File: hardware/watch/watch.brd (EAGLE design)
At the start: 36 x 35.5 mm, 92 parts, among them IC1 Digikey: WM9203CT-ND, IC2 MPR121, Q1 NTS4173, Q3 NTS4173, Q4 NTS4173, U1 Value, U10 2450BM14E0003, U11 MCP73831, U12 ML8511-UV-SENSORSMD, U13 LIGHTSENSORALS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

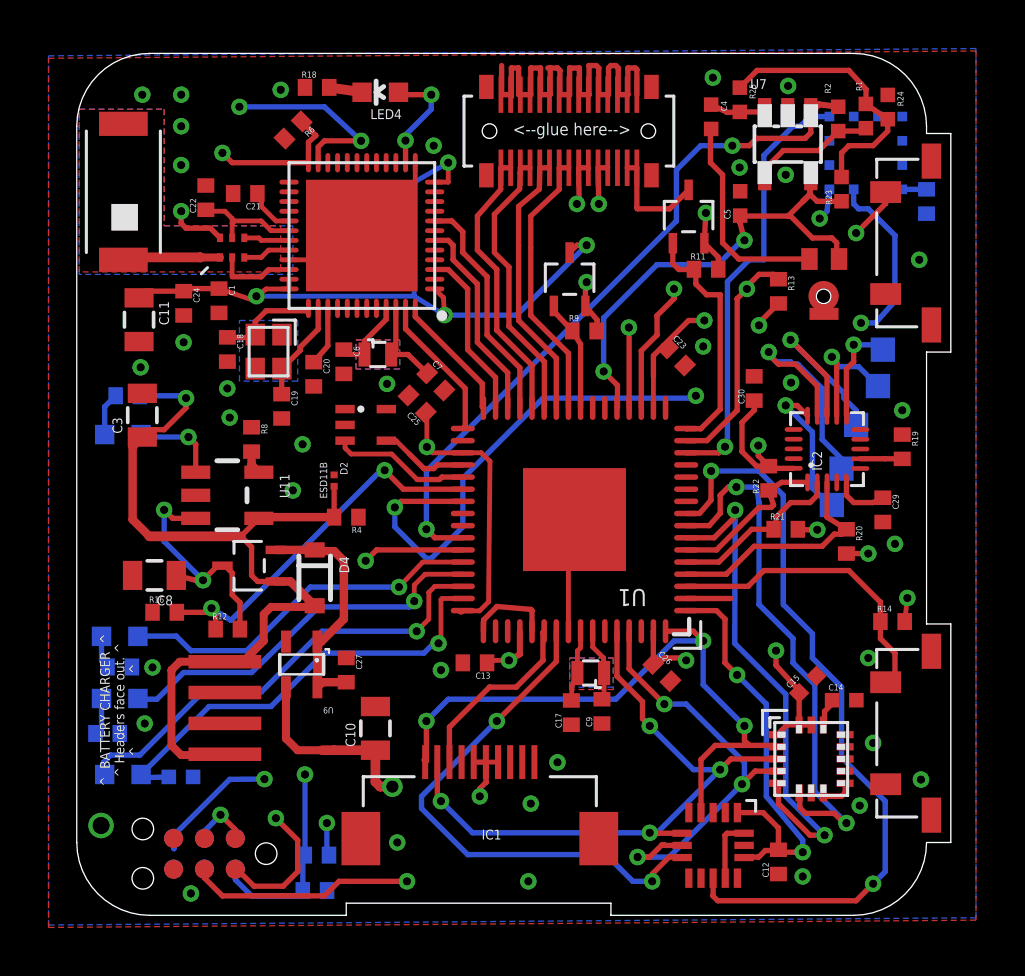
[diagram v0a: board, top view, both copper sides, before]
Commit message: New hardware revision, better connector.
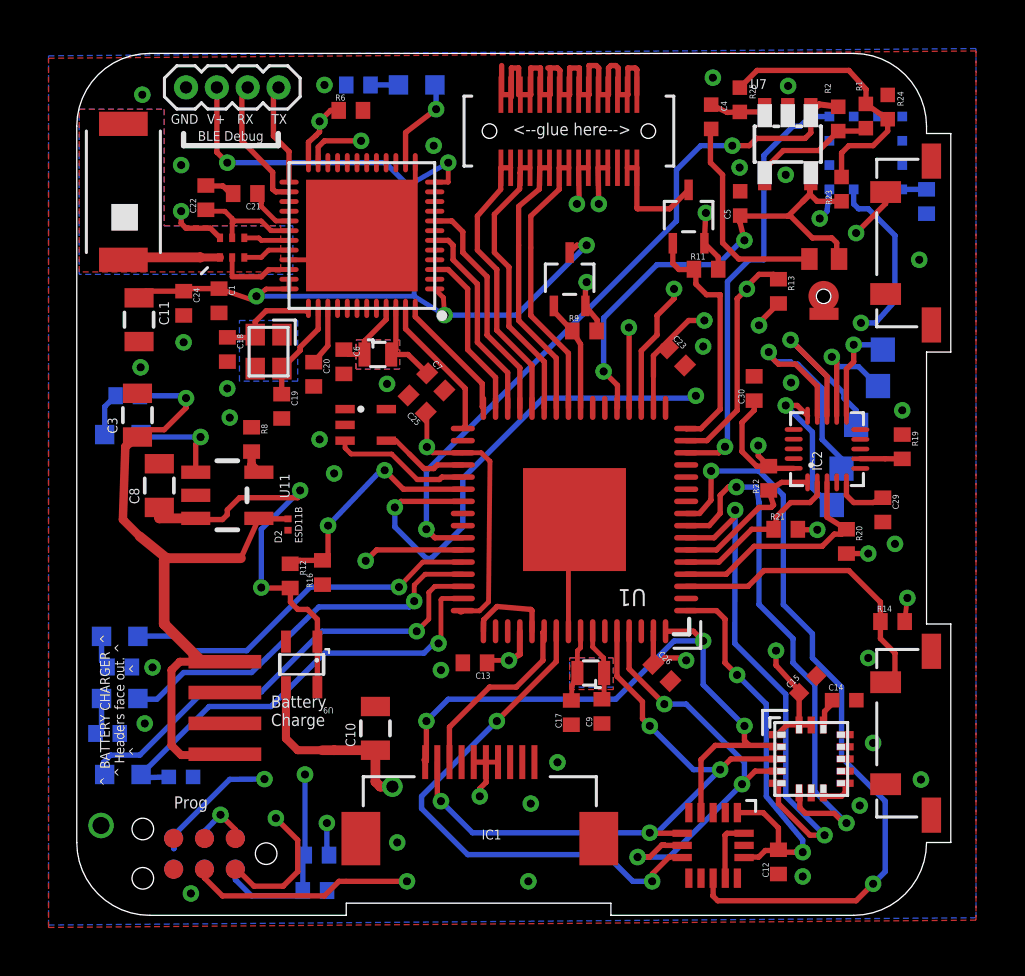
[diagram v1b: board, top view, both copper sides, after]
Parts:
- removed C27: 2.2uF, tiny_passives:0402
- removed D4: BAT20J, SparkFun-DiscreteSemi:SOD-323
- removed Q4: NTS4173, nts4173p:SC-70-3
- removed R4: 220k, tiny_passives:0402
- added JP2: (no value), SparkFun-Connectors:1X04-1.27MM
- moved R16 6.70 mm to (10.1, 14.1), turned to 90 degrees
- moved C8 3.71 mm to (3.40, 17.7), turned to 90 degrees
- moved R12 3.38 mm to (8.79, 14.0), turned to 270 degrees
- moved D2 2.62 mm to (8.70, 16.1), turned to 90 degrees
- moved R6 2.51 mm to (11.3, 33.2), turned to 0 degrees
- moved R18 1.70 mm to (11.6, 34.2), flipped to the bottom, turned to 180 degrees
- moved LED4 1.53 mm to (14.0, 34.2), flipped to the bottom, turned to 270 degrees
- moved C3 0.20 mm to (2.50, 20.6)
- renumbered U$1 to JP3
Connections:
- removed net !GYRO_ENABLE: U1.2
- removed net V_PRE_REG: C27.2, D4.C, Q4.P2, U9.1, U9.4
- new net DEBUG_BLE_RX: JP2.3, U4.26
- new net DEBUG_BLE_TX: JP2.4, U4.25
- net GND: now also JP2.1; no longer C27.1, R4.1
- net V+: now also JP2.2
- net VBAT: now also U9.1, U9.4; no longer Q4.P3
- net VIN: no longer D4.A, Q4.P1, R4.2
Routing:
- net V+: track 31.8 -> 43.1 mm, vias 4 -> 5
- net V_PRE_REG: track 10.0 -> 0.00 mm
- net SWDIO/!RESET: track 50.2 -> 41.2 mm, vias 4 -> 3
- net ADC_BATT: track 15.8 -> 9.73 mm
- net DEBUG_BLE_RX: track 0.00 -> 5.52 mm
- net DEBUG_BLE_TX: track 0.00 -> 4.25 mm
- net VIN: track 36.4 -> 32.2 mm
- net VBAT: track 35.6 -> 39.3 mm
- net SWDCLK: track 55.6 -> 52.3 mm
- net !GYRO_ENABLE: track 1.85 -> 0.00 mm
- net GND: track 47.7 -> 49.0 mm, vias 35 -> 33
- net N$37: track 4.61 -> 3.85 mm, vias 2 -> 1
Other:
- board text added: "BLE Debug"
- board text added: "Battery Charge"
- board text added: "GND"
- board text added: "Prog"
- board text added: "RX"
- board text added: "TX"
- board text added: "V+"
